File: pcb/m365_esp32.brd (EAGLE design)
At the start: 23 x 72 mm, 45 parts, among them J2 105133-0011, Q1 32768kHz, T2 BCX19SMD

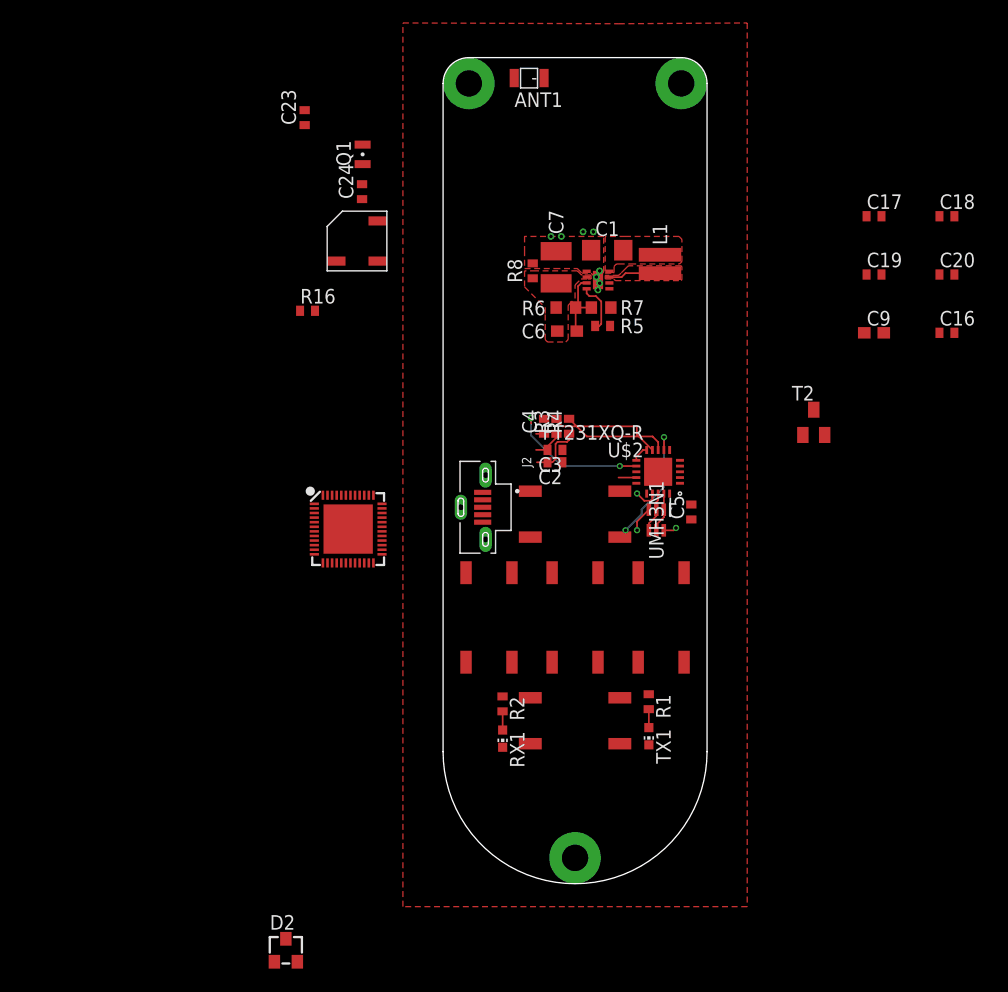
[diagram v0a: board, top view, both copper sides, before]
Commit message: Placed the buttons, center button multiplexer, usb interface, 3v3 regulator
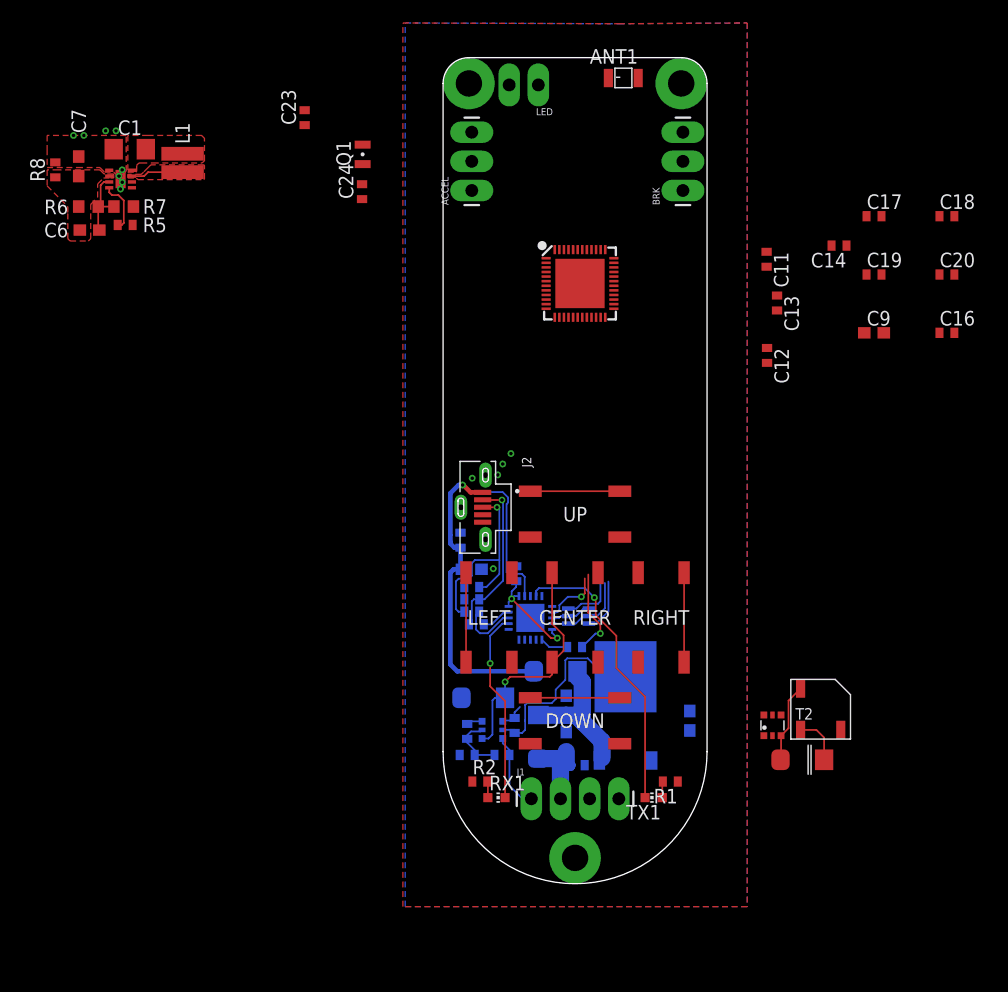
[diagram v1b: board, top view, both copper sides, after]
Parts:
- added ACCEL, BRK: (no value), SparkFun-Connectors:1X03_LONGPADS
- added C10, C15, C22, C8: 22u, eagle-ltspice:C0603
- added C11, C12, C13, C14, C21: 0.1uF, eagle-ltspice:C0402
- added D1, D3, D4: SMAFJ75A, my-lib:SMAFJ75A
- added J1: (no value), SparkFun-Connectors:1X04_LONGPADS
- added LED: (no value), SparkFun-Connectors:1X02_LONGPADS
- added R10, R12: 866k, eagle-ltspice:R0402
- added R11: 180k, eagle-ltspice:R0402
- added R9: 6.65k, eagle-ltspice:R0402
- added T1: L2N7002DW1T1G, nxp_60_1_1:SOT363
- added U$7: UZ1085L-33-TN3-R, my-lib:TO-252-2
- C4: value 10nF -> 0.1uF
- C7: device eagle-ltspice:C1210 -> eagle-ltspice:C0603
- D2: value (none) -> SMAFJ75A; device diode:TO236 -> my-lib:SMAFJ75A
- T2: value BCX19SMD -> L2N7002DW1T1G; device transistor-npn:SOT23-BEC -> nxp_60_1_1:SOT363
- moved U$8 57.4 mm to (21.4, 15.2), turned to 270 degrees
- moved D2 48.0 mm to (19.8, 10.8)
- moved R8 42.5 mm to (-45.3, 62.2)
- moved BOOST 42.5 mm to (-39.6, 61.4)
- moved C6 42.5 mm to (-42.3, 57.0)
- moved C7 42.5 mm to (-43.2, 62.5)
- moved L1 42.5 mm to (-34.2, 62.8)
- moved R5 42.5 mm to (-39.2, 57.4)
- moved R6 42.5 mm to (-42.4, 59.0)
- moved R7 42.5 mm to (-39.3, 59.0)
- moved C1 42.5 mm to (-38.8, 64.0)
- moved R16 37.4 mm to (-0.04, 20.6), flipped to the bottom
- moved U$1 29.4 mm to (0.43, 52.3)
- moved T2 26.6 mm to (17.2, 13.8)
- moved R3 18.6 mm to (-8.60, 22.6), flipped to the bottom, turned to 180 degrees
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- renumbered U$12 to CENTER, U$13 to UP, U$14 to LEFT, U$15 to DOWN, U$16 to RIGHT
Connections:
- removed net VUSB: C4.1, J2.1, R1.1, R2.1, U$2.P$12
- new net 5V_IN: C15.1, C21.1, D3.P$2, J1.2
- new net 5V_USB: C22.1, C4.1, D4.P$2, J2.1, R1.1, R2.1, U$2.P$12
- new net BUZZER: T2.5
- new net DATA: J1.3
- new net N$10: R9.1, T1.6
- new net N$11: CENTER.P$1, CENTER.P$4, D1.P$1, T1.4
- new net N$12: D2.P$2, T2.3, U$8.P$1
- new net N$5: R11.2, R12.1, R9.2, T1.5
- net 3V3: now also ACCEL.3, BRK.3, C8.1, D2.P$1, R10.2, T1.2, U$7.3, U$8.P$2
- net 42V: now also J1.1, R12.2, T1.3; no longer CENTER.P$1, CENTER.P$4, D2.C
- net 5V: now also C10.1, D3.P$1, D4.P$1, U$7.2
- net A0: now also ACCEL.2
- net A1: now also BRK.2
- net D1: now also D1.P$2; no longer D2.A
- net D13-SCK: now also C13.2, DOWN.P$1, DOWN.P$4; no longer RIGHT.P$1, RIGHT.P$4
- net D2: now also C14.2, UP.P$1, UP.P$4; no longer DOWN.P$1, DOWN.P$4
- net D3: now also C11.1, LEFT.P$1, LEFT.P$4; no longer UP.P$1, UP.P$4
- net D4-MOSI: now also C12.1, RIGHT.P$1, RIGHT.P$4; no longer LEFT.P$1, LEFT.P$4
- net FRONT_LED: now also LED.1
- net GND: now also ACCEL.1, BRK.1, C10.2, C11.2, C12.2, C13.1, C14.1, C15.2, C21.2, C22.2, C8.2, J1.4, LED.2, R10.1, R11.1, T1.1, T2.1, T2.2, T2.4, T2.6, U$7.1
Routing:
- net 5V_USB: track 0.00 -> 41.8 mm, vias 0 -> 1
- net CBUS4: track 1.55 -> 25.2 mm, vias 0 -> 1
- net 3V3: track 0.00 -> 21.4 mm
- net N$11: track 0.00 -> 20.7 mm, vias 0 -> 1
- net VUSB: track 13.1 -> 0.00 mm, vias 2 -> 0
- net USB-DATA_P: track 4.92 -> 17.8 mm, vias 0 -> 1
- net 5V: track 0.00 -> 12.8 mm
- net USB-DATA_M: track 2.72 -> 14.4 mm, vias 0 -> 1
- net N$6: track 1.45 -> 9.54 mm, vias 0 -> 2
- net 5V_IN: track 0.00 -> 8.02 mm
- net D4-MOSI: track 0.00 -> 7.80 mm
- net D3: track 0.00 -> 7.80 mm
- net D2: track 0.00 -> 7.80 mm
- net D13-SCK: track 0.00 -> 7.80 mm
- net N$1: track 0.00 -> 7.65 mm, vias 0 -> 1
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- added copper zone on layer 16, net GND

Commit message: Finished placing all components on the board
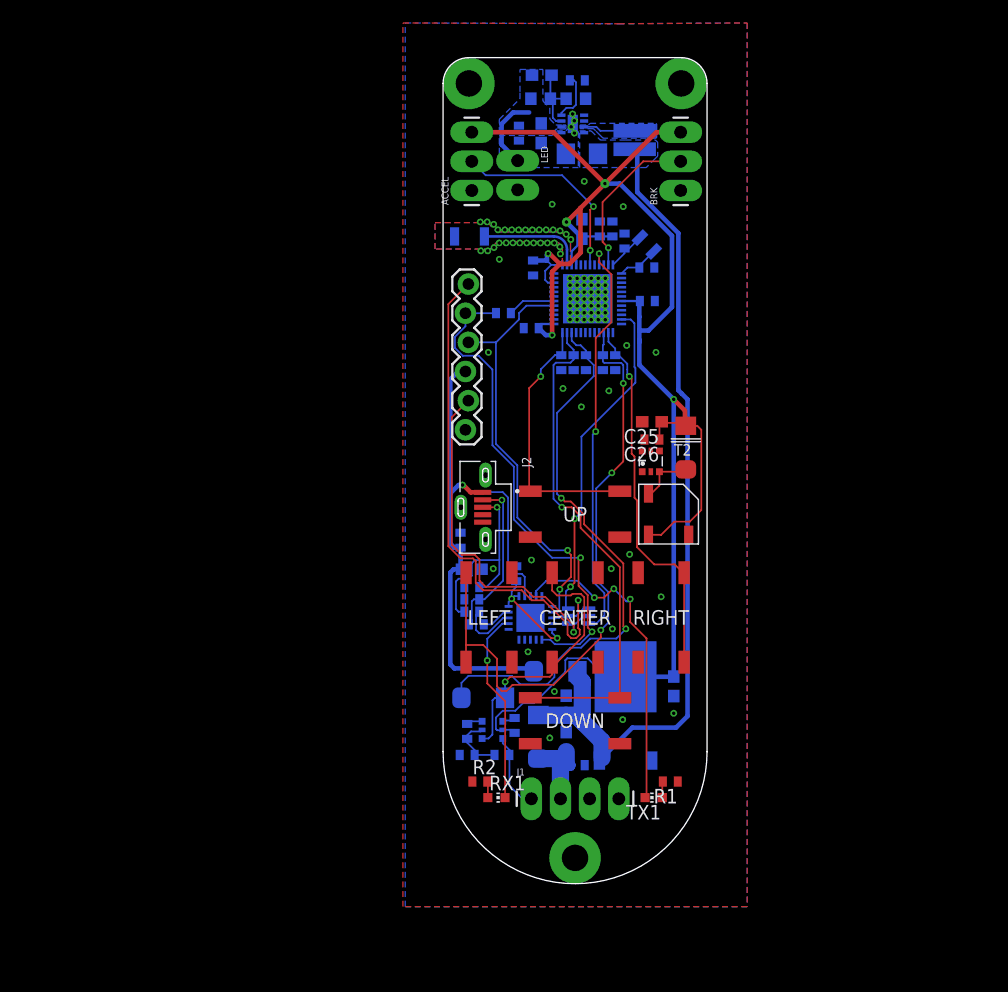
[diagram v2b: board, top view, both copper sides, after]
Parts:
- added C25: 22u, eagle-ltspice:C0603
- added C26, C27: 0.1uF, eagle-ltspice:C0402
- added J3: (no value), SparkFun-Connectors:1X06_LOCK
- moved C6 41.6 mm to (-2.90, 70.5), flipped to the bottom, turned to 180 degrees
- moved R5 41.4 mm to (0.20, 70.0), flipped to the bottom, turned to 0 degrees
- moved R8 40.5 mm to (-4.89, 65.4), flipped to the bottom, turned to 90 degrees
- moved R6 40.5 mm to (-3.00, 68.4), flipped to the bottom, turned to 0 degrees
- moved R7 40.5 mm to (0.07, 68.4), flipped to the bottom, turned to 0 degrees
- moved C7 40.4 mm to (-2.95, 65.4), flipped to the bottom, turned to 270 degrees
- moved BOOST 39.7 mm to (-0.20, 66.2), flipped to the bottom, turned to 180 degrees
- moved L1 39.5 mm to (5.20, 64.8), flipped to the bottom, turned to 180 degrees
- moved C1 39.4 mm to (0.60, 63.6), flipped to the bottom, turned to 180 degrees
- moved C18 37.5 mm to (-3.82, 48.4), flipped to the bottom
- moved C20 36.1 mm to (-3.66, 53.6), flipped to the bottom, turned to 270 degrees
- moved C16 30.5 mm to (3.25, 57.0), flipped to the bottom, turned to 90 degrees
- moved C23 29.9 mm to (4.31, 56.0), flipped to the bottom
- moved R16 29.8 mm to (-6.24, 49.7)
- moved D2 29.0 mm to (9.65, 38.0), turned to 90 degrees
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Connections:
- net D3 renamed BTN_LEFT
- net D4-MOSI renamed BTN_RIGHT
- removed net A0: ACCEL.2, U$1.5
- removed net A1: BRK.2, U$1.6
- removed net D0: U$1.36
- removed net D1: D1.P$2, U$1.35
- removed net D13-SCK: C13.2, DOWN.P$1, DOWN.P$4, U$1.24
- removed net D14: U$1.32
- removed net D15: U$1.33
- removed net D2: C14.2, U$1.34, UP.P$1, UP.P$4
- removed net D5-MISO: U$1.14
- removed net D6: U$1.15
- removed net D7: U$1.16
- removed net RGB_B: U$1.31
- removed net RGB_G: U$1.30
- removed net RGB_R: U$1.29
- removed net SCL: U$1.40
- removed net SDA: U$1.43
- new net BTN_CENTER: C27.1, D1.P$2, U$1.34
- new net BTN_DOWN: C13.2, DOWN.P$1, DOWN.P$4, U$1.35
- new net BTN_UP: C14.2, U$1.36, UP.P$1, UP.P$4
- net !DTR1: now also J3.6
- net !RTS1: now also J3.2
- net 3V3: now also C25.1, C26.1
- net 5V_USB: now also J3.3
- net A2: now also ACCEL.2
- net A5: now also BRK.2
- net GND: now also C25.2, C26.2, C27.2, J3.1
- net RX0: now also J3.4
- net TX0: now also J3.5
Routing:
- net 3V3: track 21.4 -> 155.0 mm, vias 0 -> 5
- net 5V: track 12.8 -> 73.4 mm
- net BTN_CENTER: track 0.00 -> 49.8 mm, vias 0 -> 2
- net BTN_LEFT: track 7.80 -> 54.4 mm, vias 0 -> 3
- net BTN_DOWN: track 0.00 -> 44.3 mm, vias 0 -> 1
- net !DTR1: track 3.54 -> 47.8 mm, vias 0 -> 1
- net TX0: track 2.47 -> 43.1 mm, vias 0 -> 2
- net RX0: track 5.07 -> 37.2 mm, vias 1 -> 2
- net RESET: track 4.73 -> 35.7 mm, vias 0 -> 2
- net !RTS1: track 7.35 -> 32.6 mm, vias 0 -> 1
- net BTN_RIGHT: track 7.80 -> 32.8 mm, vias 0 -> 1
- net GPIO0: track 5.17 -> 28.9 mm, vias 0 -> 2
- net BTN_UP: track 0.00 -> 23.2 mm, vias 0 -> 1
- net A2: track 0.00 -> 17.4 mm, vias 0 -> 2
- net A5: track 0.00 -> 14.0 mm, vias 0 -> 1
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- added copper zone on layer 16, net 5V
- added copper zone on layer 16, net FRONT_LED
- added copper zone on layer 16, net N$7
- added copper zone on layer 16, net NO_GND1
- added copper zone on layer 1, net NO_GND2
- removed copper zone on layer 1, net 5V
- removed copper zone on layer 1, net FRONT_LED
- removed copper zone on layer 1, net N$7
